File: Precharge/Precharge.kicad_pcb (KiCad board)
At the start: 2 copper layers, 85 x 85 mm, 70 parts, among them J1 Conn_01x02, J2 Conn_01x02, J3 Molex MicroFit, J4 Conn_02x03_Counter_Clockwise, K1 KT12-1A-40L-THT, Q1 AO3400A, Q2 AO3400A, Q3 AO3400A, U1 LM393, U2 4N35, U3 4N35

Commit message: Precharge modifications
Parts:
- removed R20, R23: 100K, Resistor_SMD:R_0603_1608Metric_Pad0.98x0.95mm_HandSolder
- added TP6: TestPoint, Connector_Pin:Pin_D1.0mm_L10.0mm, F.Cu at (76.6, 87.5)
- added TP7: GLV-, Connector_Pin:Pin_D1.0mm_L10.0mm, F.Cu at (151.3, 109.4)
- Q1: value AO3400A -> CJ2310
- R33, R34, R35, R36, R37, R38: value 10K -> 8.6K
- moved TP5 12.1 mm to (151.3, 105.9)
- moved R17 8.08 mm to (140.4, 108.9)
- moved TP4 5.58 mm to (151.2, 102.5)
- moved R38 1.26 mm to (140.4, 110.7), turned to 0 degrees
- moved R33 0.78 mm to (137.4, 115.2)
- moved R28 0.30 mm to (136.5, 128.6)
- moved R35 0.22 mm to (136.5, 126.8)
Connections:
- net /AIR+_Con renamed /AIR+_GND
- D2 pad 1: /PRECH_PWR -> GLV+
- J3 pad 1: GLV- -> GLV+
- K1 pad COIL2: /PRECH_PWR -> GLV+
- R16 pad 2: /PRECH_PWR -> GLV+
- R17 pad 1: /PRECH_PWR -> GLV+
- R19 pad 1: /PRECH_PWR -> GLV+
- R26 pad 1: /PRECH_PWR -> GLV+
- R28 pad 1: /PRECH_PWR -> GLV+
- R30 pad 1: /PRECH_PWR -> GLV+
- R32 pad 1: /PRECH_PWR -> GLV+
- U2 pad 5: /PRECH_PWR -> GLV+
- U3 pad 5: /PRECH_PWR -> GLV+
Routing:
- net GLV+: track 0.00 -> 155.2 mm, vias 0 -> 6
- net /PRECH_PWR: track 162.4 -> 57.5 mm, vias 6 -> 2
- net Net-(D4-A): track 60.2 -> 71.1 mm, vias 0 -> 1
- net /PreCh_Complt: track 65.6 -> 59.3 mm, vias 2 -> 4
- net /AIR-_Out: track 74.1 -> 77.8 mm, vias 0 -> 2
- net HV-: track 176.3 -> 179.7 mm, vias 240 -> 261
- net /Precharge: track 22.2 -> 19.8 mm
- net /PreCh_Int: track 64.7 -> 66.5 mm
- net Net-(J2-Pin_2): track 53.0 -> 54.6 mm
- net Net-(D1-K): track 9.77 -> 11.3 mm
- net GLV-: track 1.41 -> 0.03 mm, vias 22 -> 30
- net /AIR+_GND: track 68.1 -> 67.0 mm, vias 2 -> 5
- net /AIR+_Out: track 95.6 -> 96.6 mm, vias 0 -> 2
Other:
- board text added: "HV-"
- board text added: "HV- nets here are for thermal management DO NOT connect to HV"
- board text added: "PC"
- board text added: "PC_S"
- board text added: "v3.4"
- board text removed: "v3.3"

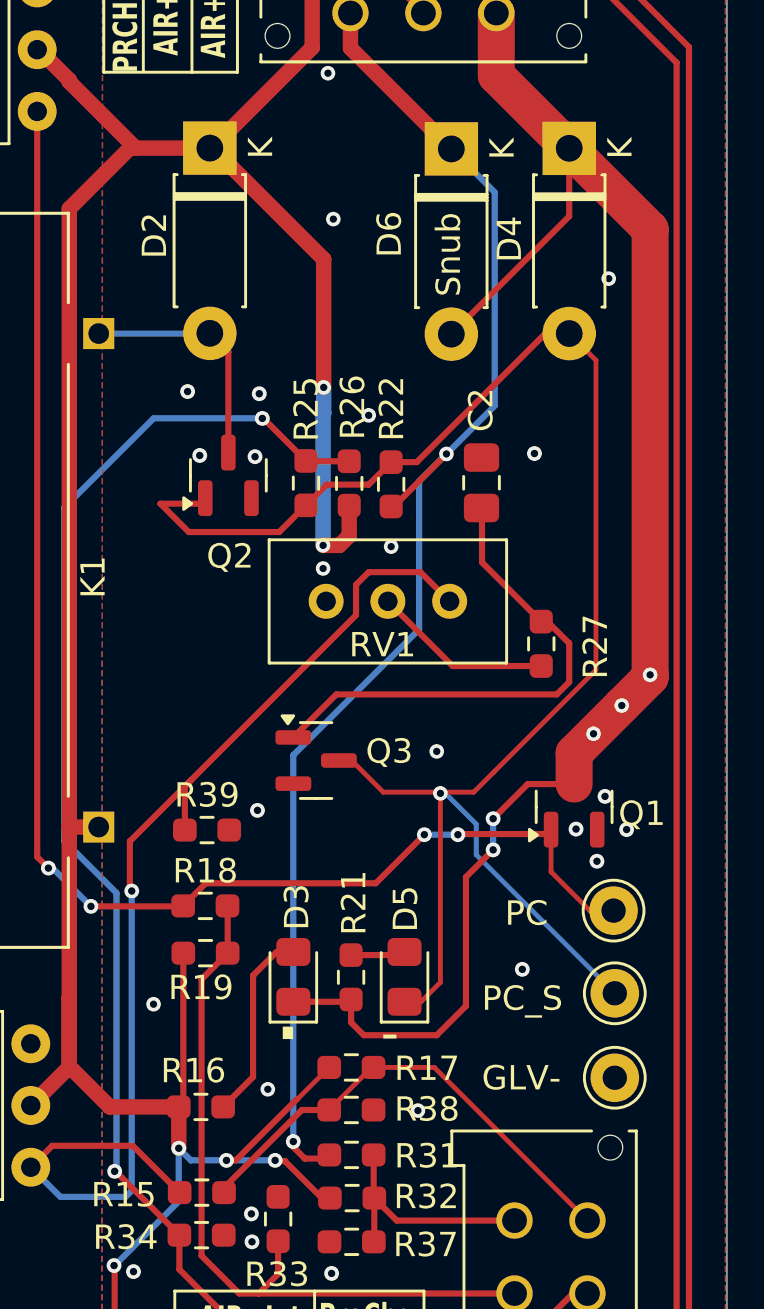
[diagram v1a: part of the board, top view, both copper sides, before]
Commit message: Modify Precharge PCB
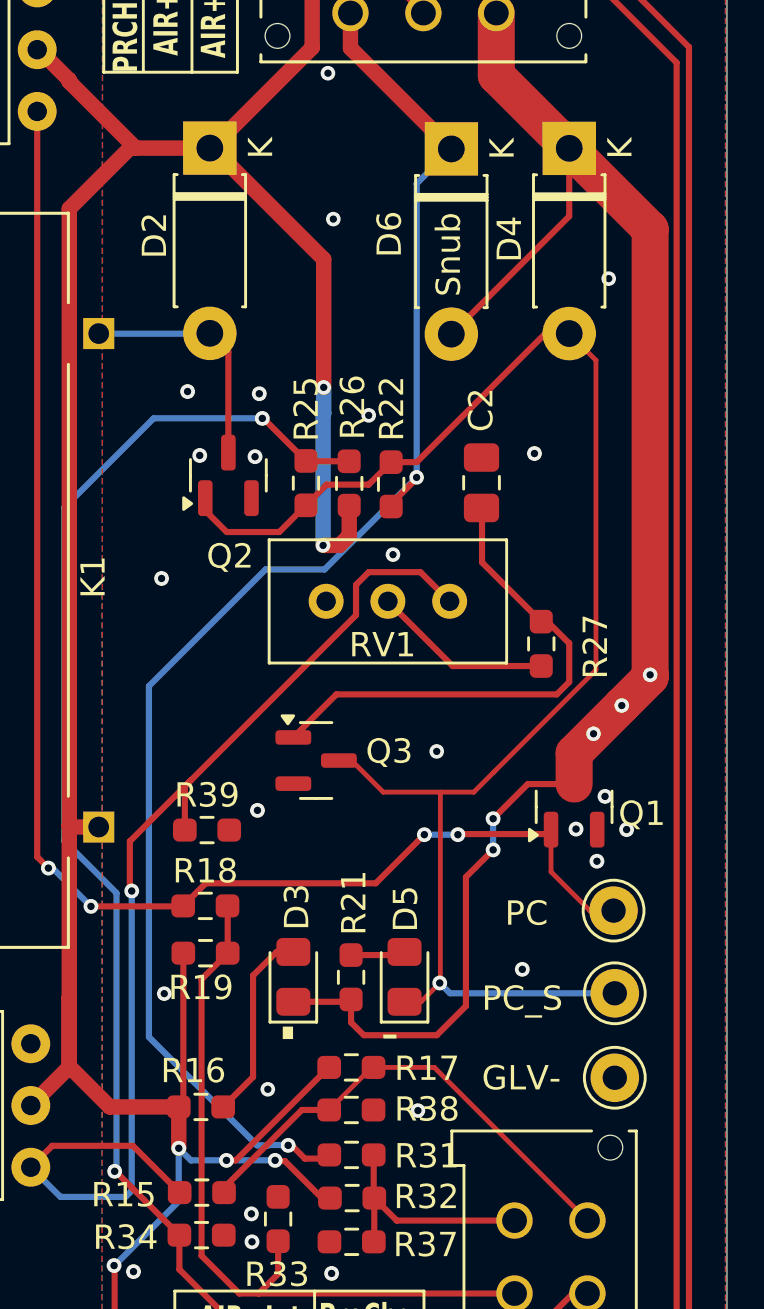
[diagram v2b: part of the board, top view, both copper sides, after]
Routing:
- net Net-(D4-A): track 71.1 -> 63.7 mm
- net /PRECH_PWR: track 57.5 -> 61.7 mm
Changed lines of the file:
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@@
 	)
 	(via
-		(at 142.079 87.514)
+		(at 142.154 87.844)
 		(size 0.6)
 		(drill 0.3)
@@
 	)
 	(via
+		(at 132.634 88.824)
+		(size 0.6096)
+		(drill 0.3048)
+		(layers "F.Cu" "B.Cu")
+		(free yes)
+		(net 2)
+	)
+	(via
 		(at 143.179 110.714)
 		(size 0.6)
@@
 	)
 	(via
-		(at 139.279 88.414)
-		(size 0.6)
-		(drill 0.3)
-		(layers "F.Cu" "B.Cu")
-		(free yes)
-		(net 2)
-	)
-	(via
 		(at 136.479 83.814)
 		(size 0.61)
@@
 	)
 	(via
-		(at 132.304 106.339)
+		(at 132.744 105.904)
 		(size 0.6)
 		(drill 0.3)
@@
 	)
 	(segment
-		(start 142.190712 85.864)
-		(end 142.079 85.864)
-		(width 0.254)
-		(layer "F.Cu")
-		(net 11)
-	)
-	(segment
-		(start 144.353212 83.7015)
-		(end 142.190712 85.864)
+		(start 137.909 112.214)
+		(end 138.054 112.214)
 		(width 0.254)
 		(layer "F.Cu")
@@
 	)
 	(segment
-		(start 142.043 85.828)
-		(end 142.079 85.864)
-		(width 0.635)
+		(start 143.126 84.712)
+		(end 142.079 85.759)
+		(width 0.254)
 		(layer "F.Cu")
 		(net 11)
 	)
 	(segment
-		(start 139.38525 112.689)
-		(end 139.53525 112.539)
+		(start 137.840892 112.145892)
+		(end 137.909 112.214)
 		(width 0.254)
 		(layer "F.Cu")
@@
 	)
 	(segment
+		(start 142.043 85.828)
+		(end 142.079 85.864)
+		(width 0.635)
+		(layer "F.Cu")
+		(net 11)
+	)
+	(segment
 		(start 138.529 112.689)
 		(end 139.38525 112.689)
@@
 	)
 	(segment
-		(start 138.054 111.989)
-		(end 138.054 112.214)
+		(start 142.079 85.759)
+		(end 142.079 85.864)
+		(width 0.254)
+		(layer "F.Cu")
+		(net 11)
+	)
+	(segment
+		(start 139.38525 112.689)
+		(end 139.53525 112.539)
+		(width 0.254)
+		(layer "F.Cu")
+		(net 11)
+	)
+	(segment
+		(start 143.126 84.666)
+		(end 143.126 84.712)
 		(width 0.254)
 		(layer "F.Cu")
@@
 	)
 	(via
-		(at 138.054 111.989)
+		(at 137.840892 112.145892)
 		(size 0.61)
 		(drill 0.305)
@@
 	)
 	(via
-		(at 144.353212 83.7015)
+		(at 143.126 84.666)
 		(size 0.6)
 		(drill 0.3)
@@
 	)
 	(segment
-		(start 146.337822 81.71689)
-		(end 146.337822 72.937822)
+		(start 136.565892 112.145892)
+		(end 132.114 107.694)
+		(width 0.254)
+		(layer "B.Cu")
+		(net 11)
+	)
+	(segment
+		(start 137.566115 112.1312)
+		(end 137.041885 112.1312)
+		(width 0.254)
+		(layer "B.Cu")
+		(net 11)
+	)
+	(segment
+		(start 136.914 88.454)
+		(end 139.338 88.454)
+		(width 0.254)
+		(layer "B.Cu")
+		(net 11)
+	)
+	(segment
+		(start 139.338 88.454)
+		(end 143.126 84.666)
 		(width 0.254)
 		(layer "B.Cu")
@@
 	)
 	(segment
-		(start 138.054 96.089)
-		(end 143.229 90.914)
+		(start 137.041885 112.1312)
+		(end 137.027193 112.145892)
 		(width 0.254)
 		(layer "B.Cu")
@@
 	)
 	(segment
-		(start 143.229 84.825712)
-		(end 144.353212 83.7015)
+		(start 137.840892 112.145892)
+		(end 137.580807 112.145892)
 		(width 0.254)
 		(layer "B.Cu")
@@
 	)
 	(segment
-		(start 144.353212 83.7015)
-		(end 146.337822 81.71689)
+		(start 143.126 84.666)
+		(end 143.126 72.582)
 		(width 0.254)
 		(layer "B.Cu")
@@
 	)
 	(segment
-		(start 138.054 111.989)
-		(end 138.054 96.089)
+		(start 137.027193 112.145892)
+		(end 136.565892 112.145892)
 		(width 0.254)
 		(layer "B.Cu")
@@
 	)
 	(segment
-		(start 146.337822 72.937822)
+		(start 143.126 72.582)
 		(end 144.554 71.154)
 		(width 0.254)
@@
 	)
 	(segment
-		(start 143.229 90.914)
-		(end 143.229 84.825712)
+		(start 137.580807 112.145892)
+		(end 137.566115 112.1312)
+		(width 0.254)
+		(layer "B.Cu")
+		(net 11)
+	)
+	(segment
+		(start 132.114 107.694)
+		(end 132.114 93.254)
+		(width 0.254)
+		(layer "B.Cu")
+		(net 11)
+	)
+	(segment
+		(start 132.114 93.254)
+		(end 136.914 88.454)
 		(width 0.254)
 		(layer "B.Cu")
@@
 	)
 	(segment
+		(start 138.575 85.8145)
+		(end 137.4755 86.914)
+		(width 0.254)
+		(layer "F.Cu")
+		(net 24)
+	)
+	(segment
 		(start 139.4255 84.964)
 		(end 141.154 84.964)
@@
 	(segment
 		(start 143.304 106.239)
-		(end 144.104 105.439)
+		(end 144.0765 105.4665)
 		(width 0.2)
 		(layer "F.Cu")
@@
 	)
 	(segment
-		(start 133.7535 86.914)
-		(end 137.4755 86.914)
+		(start 134.432 86.032)
+		(end 134.432 85.5195)
 		(width 0.254)
 		(layer "F.Cu")
@@
 	)
 	(segment
-		(start 138.575 85.8145)
-		(end 139.4255 84.964)
+		(start 135.314 86.914)
+		(end 134.432 86.032)
 		(width 0.254)
 		(layer "F.Cu")
@@
 	)
 	(segment
-		(start 132.588 85.7485)
-		(end 133.7535 86.914)
+		(start 138.575 85.8145)
+		(end 139.4255 84.964)
 		(width 0.254)
 		(layer "F.Cu")
@@
 	)
 	(segment
-		(start 144.104 97.664)
-		(end 144.104 97.614)
-		(width 0.2)
-		(layer "F.Cu")
-		(net 24)
-	)
-	(segment
 		(start 150.503999 92.58787)
 		(end 146.340935 96.750935)
@@
 	)
 	(segment
-		(start 137.4755 86.914)
-		(end 138.575 85.8145)
-		(width 0.254)
-		(layer "F.Cu")
-		(net 24)
-	)
-	(segment
 		(start 149.404 78.749)
 		(end 148.419 78.749)
@@
 	)
 	(segment
-		(start 132.588 85.7485)
-		(end 134.203 85.7485)
-		(width 0.254)
+		(start 144.0765 105.4665)
+		(end 144.104 105.439)
+		(width 0.2)
 		(layer "F.Cu")
 		(net 24)
@@
 	)
 	(segment
-		(start 134.203 85.7485)
-		(end 134.432 85.5195)
-		(width 0.254)
-		(layer "F.Cu")
-		(net 24)
-	)
-	(segment
 		(start 144.104 105.439)
 		(end 144.104 97.664)
@@
 		(net 24)
 	)
-	(via
-		(at 144.104 97.664)
-		(size 0.6)
-		(drill 0.3)
-		(layers "F.Cu" "B.Cu")
-		(net 24)
-	)
 	(segment
-		(start 145.579 98.929998)
-		(end 144.313002 97.664)
-		(width 0.2)
-		(layer "B.Cu")
+		(start 137.4755 86.914)
+		(end 135.314 86.914)
+		(width 0.254)
+		(layer "F.Cu")
 		(net 24)
 	)
-	(segment
-		(start 145.579 100.189)
-		(end 145.579 98.929998)
-		(width 0.2)
-		(layer "B.Cu")
+	(via
+		(at 144.0765 105.4665)
+		(size 0.6096)
+		(drill 0.3048)
+		(layers "F.Cu" "B.Cu")
 		(net 24)
 	)
 	(segment
 		(start 151.279 105.889)
-		(end 145.579 100.189)
-		(width 0.2)
+		(end 144.499 105.889)
+		(width 0.254)
 		(layer "B.Cu")
 		(net 24)
 	)
 	(segment
-		(start 144.313002 97.664)
-		(end 144.104 97.664)
-		(width 0.2)
+		(start 144.499 105.889)
+		(end 144.0765 105.4665)
+		(width 0.254)
 		(layer "B.Cu")
 		(net 24)
@@
 	)
 	(segment
+		(start 139.510532 108.939)
+		(end 139.529 108.939)
+		(width 0.254)
+		(layer "F.Cu")
+		(net 41)
+	)
+	(segment
 		(start 130.704 117.064)
 		(end 130.704 125.639)
@@
 	(segment
 		(start 135.685532 112.764)
-		(end 138.215533 110.234)
+		(end 139.510532 108.939)
 		(width 0.254)
 		(layer "F.Cu")
@@
 	)
 	(segment
-		(start 135.304 112.764)
-		(end 135.685532 112.764)
-		(width 0.254)
-		(layer "F.Cu")
-		(net 41)
-	)
-	(segment
 		(start 139.53525 114.289)
 		(end 139.56025 114.314)
@@
 	)
 	(segment
-		(start 138.234 110.234)
-		(end 139.529 108.939)
-		(width 0.2)
-		(layer "F.Cu")
-		(net 41)
-	)
-	(segment
 		(start 133.3415 110.564)
 		(end 133.3415 112.264)
@@
 	)
 	(segment
-		(start 138.215533 110.234)
-		(end 138.234 110.234)
-		(width 0.2)
-		(layer "F.Cu")
-		(net 41)
-	)
-	(segment
 		(start 134.654 71.154)
 		(end 134.62 71.12)
@@
 		(width 0.254)
 		(layer "F.Cu")
+		(net 41)
+	)
+	(segment
+		(start 135.304 112.764)
+		(end 135.685532 112.764)
+		(width 0.254)
+		(layer "F.Cu")

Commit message: Save corrupted files and new modifications
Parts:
- moved U1 0.27 mm to (80.3, 67.3)
- renumbered D6 to D5, D5 to D6, R39 to R15, R18 to R17, R22 to R18, R33 to R20, R24 to R22, R28 to R23, R35 to R24, R34 to R27, R27 to R28, R15 to R29, R29 to R30, R17 to R31, R38 to R32, R30 to R33, R36 to R34, R31 to R35, R32 to R36, TP6 to TP3, TP3 to TP4, TP4 to TP5, TP7 to TP6, TP5 to TP7, U2 to U3, U3 to U4
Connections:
- net /PRECH_PWR renamed /AIR_Sup+
